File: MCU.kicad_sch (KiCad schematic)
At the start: 28 parts, among them J1 Conn_cJTag_TC2030-NL, Q1 DMN2300UFB4-7B, U2 CC2640R2FRSMR

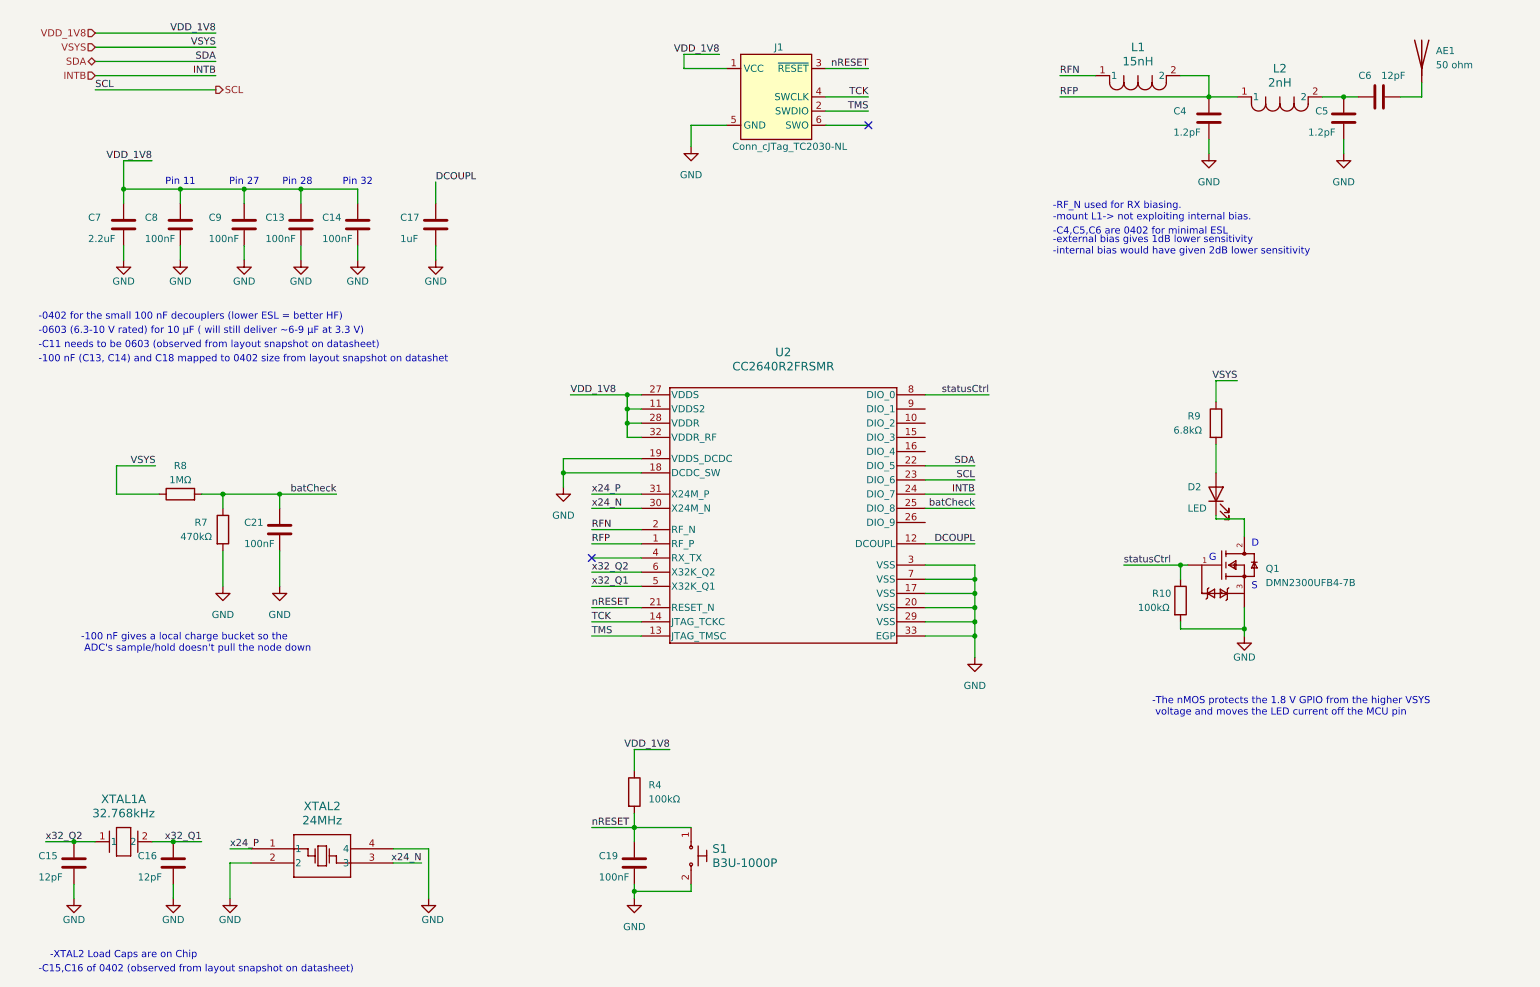
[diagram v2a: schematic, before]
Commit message: finished associating each component of each sheet of schematic to relative footprint. filled in first version field for BOM. Provided organized hierechical level directories for all the datasheets for each used component.
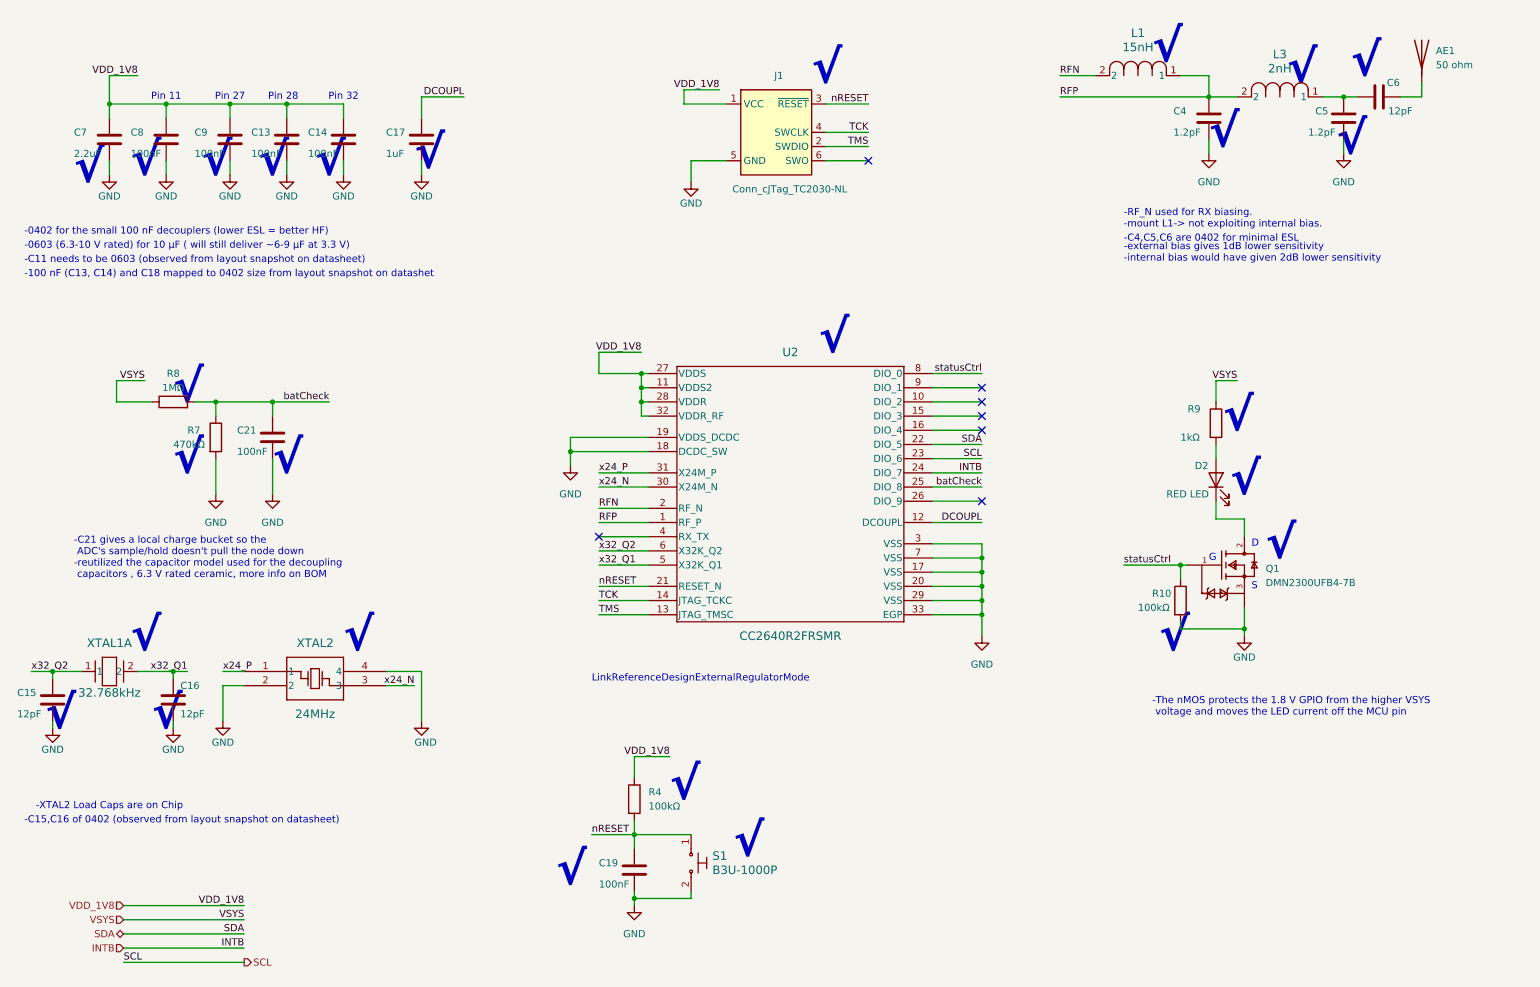
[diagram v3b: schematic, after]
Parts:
- removed L1: 15nH, IND_LQG15HN_02_MUR, symbol 15nH_inductor_local:LQG15HS15NJ02D
- removed L2: 2nH, IND_LQG15_MUR, symbol 2nH_inductor_local:LQG15HS2N0S02D
- added L1: 15nH, Inductor_SMD_local:L_0402_1005M_Murata-LQG15HS, symbol inductor_local:LQG15HS2N0S02D
- added L3: 2nH, Inductor_SMD_local:L_0402_1005M_Murata-LQG15HS, symbol inductor_local:LQG15HS2N0S02D
- AE1: MANUFACTURER (none) -> -; MPN (none) -> -; Package (none) -> -; Price (none) -> -; rohs (none) -> -; vendor (none) -> -
- C13, C14, C19, C21, C8, C9: footprint (none) -> Capacitor_SMD_local:C_0402_1005Metric; MANUFACTURER (none) -> Murata Electronics; MPN (none) -> GRM155R70J104KA01D; Package (none) -> 0402; Price (none) -> 0.09; mounting type (none) -> SMD; rohs (none) -> yes; vendor (none) -> DigiKey; vendor part number (none) -> 490-6319-1-ND
- C15, C16, C6: footprint (none) -> Capacitor_SMD_local:C_0402_1005Metric; MANUFACTURER (none) -> Johanson Technology Inc.; MPN (none) -> QSCF500Q120J1GV001T; Package (none) -> 0402; Price (none) -> 0.15; mounting type (none) -> SMD; rohs (none) -> yes; vendor (none) -> DigiKey; vendor part number (none) -> 712-QSCF500Q120J1GV001TCT-ND
- C17: footprint (none) -> Capacitor_SMD_local:C_0402_1005Metric; MANUFACTURER (none) -> YAGEO; MPN (none) -> CC0402KRX5R6BB105; Package (none) -> 0402; Price (none) -> 0.09; mounting type (none) -> SMD; rohs (none) -> yes; vendor (none) -> DigiKey; vendor part number (none) -> 311-1439-1-ND
- C4, C5: footprint (none) -> Capacitor_SMD_local:C_0402_1005Metric; MANUFACTURER (none) -> Murata Electronics; MPN (none) -> GRM1555C1H1R2BA01D; Package (none) -> 0402; Price (none) -> 0.09; mounting type (none) -> SMD; rohs (none) -> yes; vendor (none) -> DigiKey; vendor part number (none) -> 490-6209-1-ND
- C7: footprint (none) -> Capacitor_SMD_local:C_0402_1005Metric; MANUFACTURER (none) -> Murata Electronics; MPN (none) -> GRM155R60J225KE95D; Package (none) -> 0402; Price (none) -> 0.1; mounting type (none) -> SMD; rohs (none) -> yes; vendor (none) -> DigiKey; vendor part number (none) -> 490-12532-1-ND
- D2: value LED -> RED LED; footprint (none) -> ul_chargingLED_SML_P11UTT86_0402_local:LED_SML-P12UT_ROM; MANUFACTURER (none) -> Rohm Semiconductor; MPN (none) -> SML-P11VTT86; Package (none) -> 0402; Price (none) -> 0.38; mounting type (none) -> SMD; rohs (none) -> yes; vendor (none) -> DigiKey; vendor part number (none) -> 846-SML-P11VTT86CT-ND
- J1: now in the parts list
- Q1: MANUFACTURER (none) -> Diodes Incorporated; MPN (none) -> DMN2300UFB4-7B; Package (none) -> 3-XFDFN; Price (none) -> 0.32; mounting type (none) -> SMD; vendor (none) -> DigiKey; vendor part number (none) -> DMN2300UFB4-7BDICT-ND
- R10, R4: footprint (none) -> Resistor_SMD_local:R_0402_1005Metric; MANUFACTURER (none) -> Stackpole Electronics Inc; MPN (none) -> RMCF0402FT100K; Package (none) -> 0402; Price (none) -> 0.09; mounting type (none) -> SMD; rohs (none) -> yes; vendor (none) -> DigiKey; vendor part number (none) -> RMCF0402FT100KCT-ND
- R7: footprint (none) -> Resistor_SMD_local:R_0402_1005Metric; MANUFACTURER (none) -> Stackpole Electronics Inc; MPN (none) -> RMCF0402FT470K; Package (none) -> 0402; Price (none) -> 0.09; mounting type (none) -> SMD; rohs (none) -> yes; vendor (none) -> DigiKey; vendor part number (none) -> RMCF0402FT470KCT-ND
- R8: footprint (none) -> Resistor_SMD_local:R_0402_1005Metric; MANUFACTURER (none) -> TE Connectivity Passive Product; MPN (none) -> CRGCQ0402F1M0; Package (none) -> 0402; Price (none) -> 0.09; mounting type (none) -> SMD; rohs (none) -> yes; vendor (none) -> DigiKey; vendor part number (none) -> A129663CT-ND
- R9: value 6.8kΩ -> 1kΩ; footprint (none) -> Resistor_SMD_local:R_0402_1005Metric; MANUFACTURER (none) -> Stackpole Electronics Inc; MPN (none) -> RMCF0402FT1K00; Package (none) -> 0402; Price (none) -> 0.09; mounting type (none) -> SMD; rohs (none) -> yes; vendor (none) -> DigiKey; vendor part number (none) -> RMCF0402FT1K00CT-ND
- S1: MANUFACTURER (none) -> Omron Electronics Inc-EMC Div; Package (none) -> -; Price (none) -> 0.85; mounting type (none) -> SMD; rohs (none) -> yes; vendor (none) -> DigiKey; vendor part number (none) -> SW1020CT-ND
- U2: footprint RSM0032B -> MCU_CC2640R2FRSMR_local:MCU_CC2640R2F_RSM0032B; MANUFACTURER (none) -> Texas Instrument; MPN (none) -> CC2640R2FRSM; Package (none) -> VQFN (32); Price (none) -> 3.73 €; mounting type (none) -> SMD; rohs (none) -> yes; vendor (none) -> Digikey; vendor part number (none) -> 296-47747-2-ND
- XTAL1: footprint XTAL_SC-20S_EPS -> ul_crystal32768_SC20S-12-5PF20PPM_local:XTAL_SC-20S_EPS; MANUFACTURER (none) -> Seiko Instruments; MPN (none) -> SC20S-12.5PF20PPM; Package (none) -> -; Price (none) -> 0.62; mounting type (none) -> SMD; rohs (none) -> yes; vendor (none) -> Digikey; vendor part number (none) -> 728-1075-2-ND
- XTAL2: footprint ECS-160-8-36-RHN-TR_ECS -> ul_24Mcrystal_ESC-240-8-36-RWN-TR_local:ECS-160-8-36-RHN-TR_ECS; MANUFACTURER (none) -> ECS Inc.; MPN (none) -> ECS-240-8-36-RWN-TR; Package (none) -> -; Price (none) -> 0.41; mounting type (none) -> SMD; rohs (none) -> yes; vendor (none) -> Digikey; vendor part number (none) -> XC2270CT-ND
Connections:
- net RFN: now also L1.2
- net RFP: now also L1.1, L3.2
- net at C5.1, C6.1: now also L3.1
- no-connect marks 2 -> 7
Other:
- note added: "-C21 gives a local charge bucket so the ADC's sample/hold doesn't pull the node down -reutilized the capacitor model used for the decoupling capacitors , 6.3 V rated ceramic, more info on BOM"
- note added: "LinkReferenceDesignExternalRegulatorMode"
- note added: "√"
- note removed: "-100 nF gives a local charge bucket so the ADC's sample/hold doesn't pull the node down"
- moved on the sheet: C13, C14, C15, C16, C17, C19, C21, C7, C8, C9, D2, J1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

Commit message: ERC step done. most important errors and warnings resolved (the ones about unspecified pins etcetra). with the occasion have done also the checking of the symbols of each component to make sure of correct type of pins.have assigned the different fields related to the first BOM to all the components. need to still assign data sheets and description fields for some components
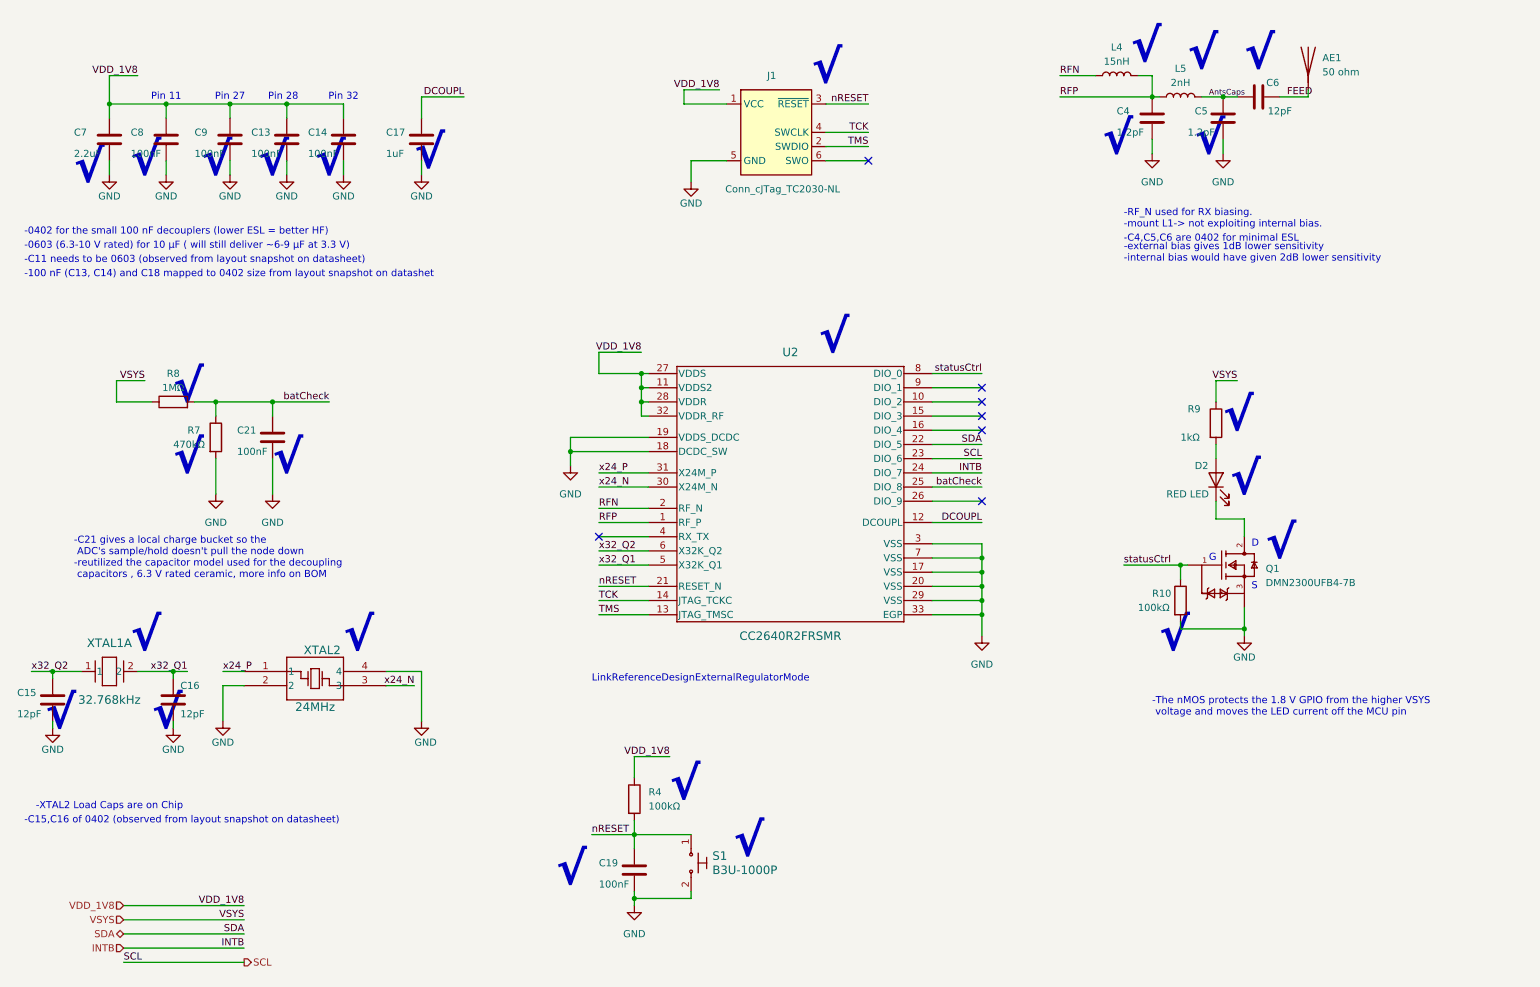
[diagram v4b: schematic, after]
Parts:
- removed L1: 15nH, Inductor_SMD_local:L_0402_1005M_Murata-LQG15HS, symbol inductor_local:LQG15HS2N0S02D
- removed L3: 2nH, Inductor_SMD_local:L_0402_1005M_Murata-LQG15HS, symbol inductor_local:LQG15HS2N0S02D
- added L4: 15nH, Inductor_SMD_local:L_0402_1005M_Murata-LQG15HS, symbol inductor_local:L
- added L5: 2nH, Inductor_SMD_local:L_0402_1005M_Murata-LQG15HS, symbol inductor_local:L
- C13, C14, C17, C19, C21, C4, C5, C8, C9, R10, R4, R7, R8, R9: Price 0.09 -> 0.09 €
- C15, C16, C6: Price 0.15 -> 0.15 €
- C7: Price 0.1 -> 0.10 €
- D2: Price 0.38 -> 0.38 €
- J1: footprint connectorTagConnect_local:Tag-Connect_TC2030-IDC-NL_2x03_P1.27mm_Vertical -> Connector:Tag-Connect_TC2030-IDC-NL_2x03_P1.27mm_Vertical
- Q1: Price 0.32 -> 0.32 €
- S1: Price 0.85 -> 0.85 €
- U2: MANUFACTURER Texas Instrument -> Texas Instruments
- XTAL1: Price 0.62 -> 0.62 €
- XTAL2: MANUFACTURER ECS Inc. -> ECS Inc.; MPN ECS-240-8-36-RWN-TR -> ECS-240-8-36-RWN-TR; Price 0.41 -> 0.41 €
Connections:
- net RFN: now also L4.1
- net RFP: now also L4.2, L5.1
- net FEED: now reaches AE1.1 (A), C6.2
- net AntsCaps: now reaches C5.1, C6.1
- net AntsCaps: now also L5.2
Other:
- moved on the sheet: AE1, C4, C5, C6

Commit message: finished layout, associated 3d models for the components, drc ran with no errors. fixed foorprints and their individaul pad dimensions (solder mask layer related, copper layer related and paste mask layer related) . EUROCIRCUITS Manufacturer report resulted in class 4C , standard and towards low cost. still needs to fix and revise silkscreen and fabrication layer
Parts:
- removed AE1: 50 ohm, symbol antenna_local:Antenna
- added AE2: Antenna_Shield, Texas_SWRA117D_2.4GHzRight_local:Texas_SWRA117D_2.4GHz_Left, symbol antenna_local:Antenna_Shield
- J1: footprint Connector:Tag-Connect_TC2030-IDC-NL_2x03_P1.27mm_Vertical -> connectorTagConnect_local:Tag-Connect_TC2030-IDC-NL_2x03_P1.27mm_Vertical
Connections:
- net FEED: now also AE2.1 (A)
- net GND: now also AE2.2 (Shield)
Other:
- note added: "-Antenna for single ended operation"
- note removed: "√"
